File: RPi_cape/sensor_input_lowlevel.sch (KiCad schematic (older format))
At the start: 37 parts, among them U17 LM2903, U4 AD8552A

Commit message: Admin (naming, license), improvements based on testing
Updated name on schematic, PCB silkscreen
Added 3 mounting holes on inside area of board for better mechanical robustness
Removed extra unused pressure sensor barb packages from library
Fixed Phoenix spring connector footprints, and added 3D models from Phoenix website
Added 3D models to TE encoder connector footprints, QFP-100 for CPLD, and 5019 testpoint
Changed DIAG_EN pin connection from valve drivers from +24V (too high) to +3.3V
Added CERN licensing terms
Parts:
- TP20: footprint TestPoint:TestPoint_Keystone_5019_Minature -> Ventilator:TestPoint_Keystone_5019_Minature
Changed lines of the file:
@@
 encoding utf-8
 Sheet 5 15
-Title "Raspberry Pi Hat for JamVent Adaptation"
+Title "GlobalVent Stand-Alone Controller"
 Date ""
-Rev "1.9"
-Comp "US JamVent Team"
-Comment1 "Don Straney"
-Comment2 ""
+Rev "1.10"
+Comp "US GlobalVent Team"
+Comment1 "Licensed under CERN-OHL-S v2"
+Comment2 "Don Straney"
 Comment3 ""
 Comment4 ""
@@
 F 0 "TP20" H 2500 7300 50  0000 R CNN
 F 1 "TestPoint_Flag" H 2456 7203 50  0001 R CNN
-F 2 "TestPoint:TestPoint_Keystone_5019_Minature" H 2700 7200 50  0001 C CNN
+F 2 "Ventilator:TestPoint_Keystone_5019_Minature" H 2700 7200 50  0001 C CNN
 F 3 "~" H 2700 7200 50  0001 C CNN
 F 4 "Keystone" H 2500 7200 50  0001 C CNN "Manufacturer"

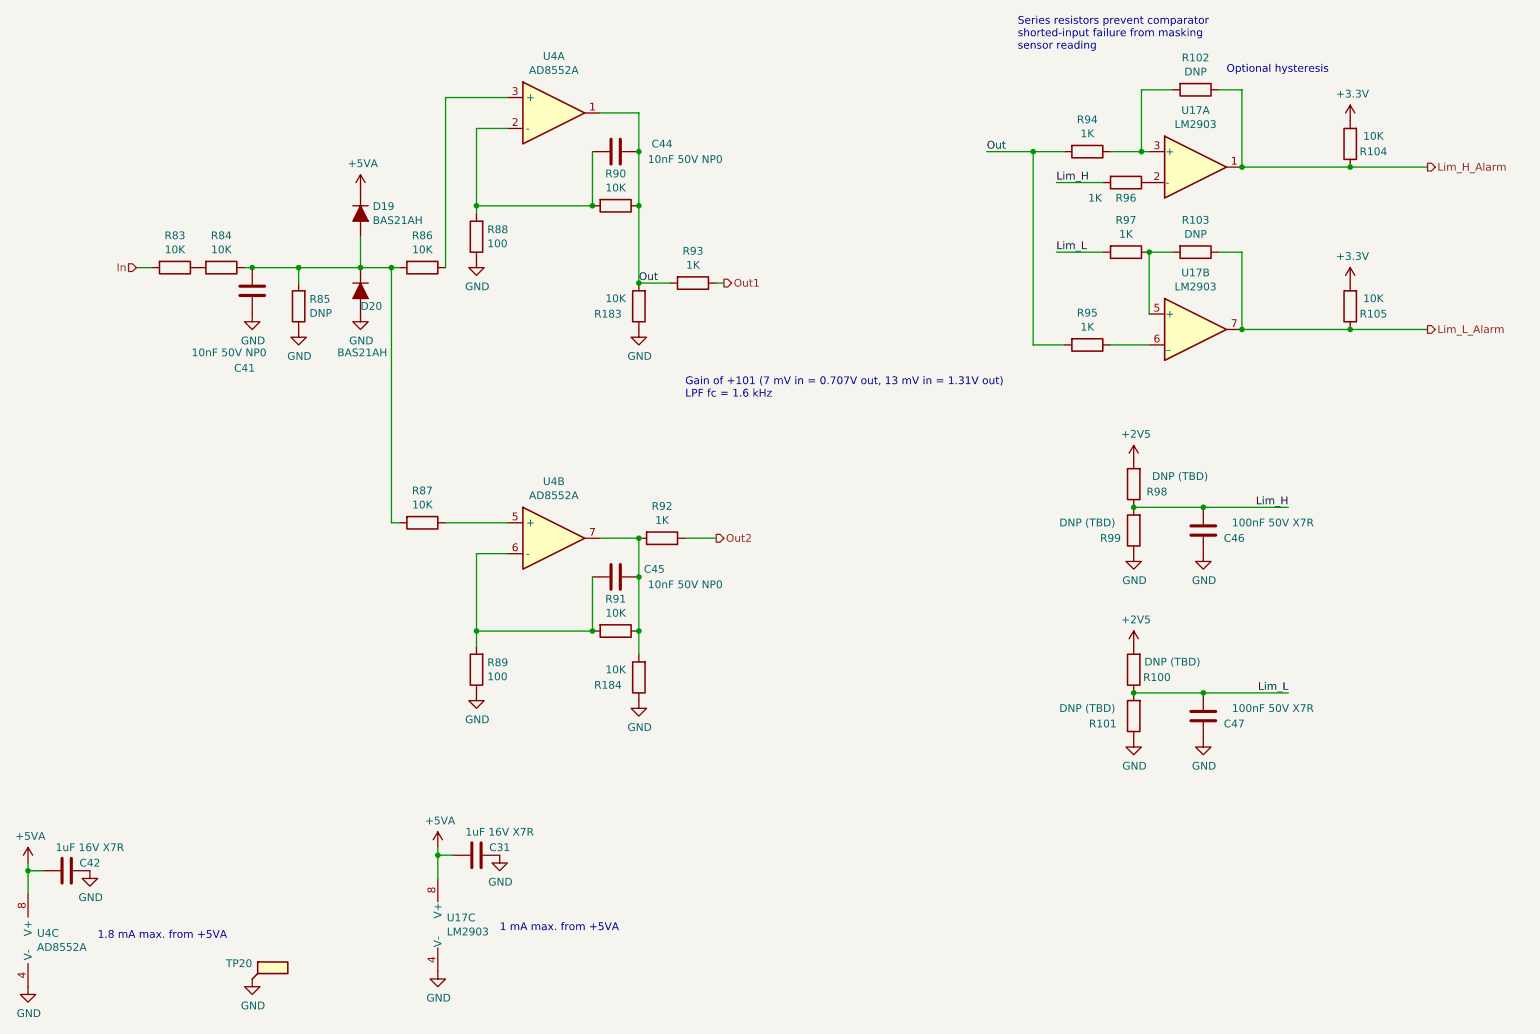
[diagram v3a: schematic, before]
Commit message: Design update based on changed software/firmware/pneumatics reqs
Swapped Max V CPLD for Max 10 FPGA
Removed +1.8V regulator and monitoring (in power-down alarm) because Max 10 FPGA has internal regulator
Changed FPGA's valve-enable pull-downs from 1K to 10K because Max 10 floats the outputs during power-up/programming (instead of Max V's internal pull-ups)
Changed low-pressure sensor from BMP388 to MS5607 for more manufacturable footprint / high availability, and moved all digital pressure sensors to daughterboard for repairability
Changed single op-amps in analog pressure sensor inputs / valve motion detect circuits to TLV6001 for better bias current, correct footprint
Removed excessive DNP components in analog pressure sensor inputs to ease routing with new op-amps
Added double-inverted hysteresis circuit to valve motion detect that won't drive U38's '+' input above the rail and cause latchup
Added optional pull-down resistors to valve-motiion-detect op-amps to allow output voltages to swing to zero
Added optional filter caps to ADC sensor inputs
Added pull-down to O2 sensor input for testing with sensor unplugged
Increased ADC input resistors (in analog sensor inputs) from 1K to 3.3K to avoid "lifting" +3.3V rail voltage in case of fault
Increased hole sizes to 3.7 mm for fitting #6 screws, to match some threaded vibration-damping bumpers from Joost
Fixed F.Fab-layer component reference text in custom footprints
Updated manufacturing files
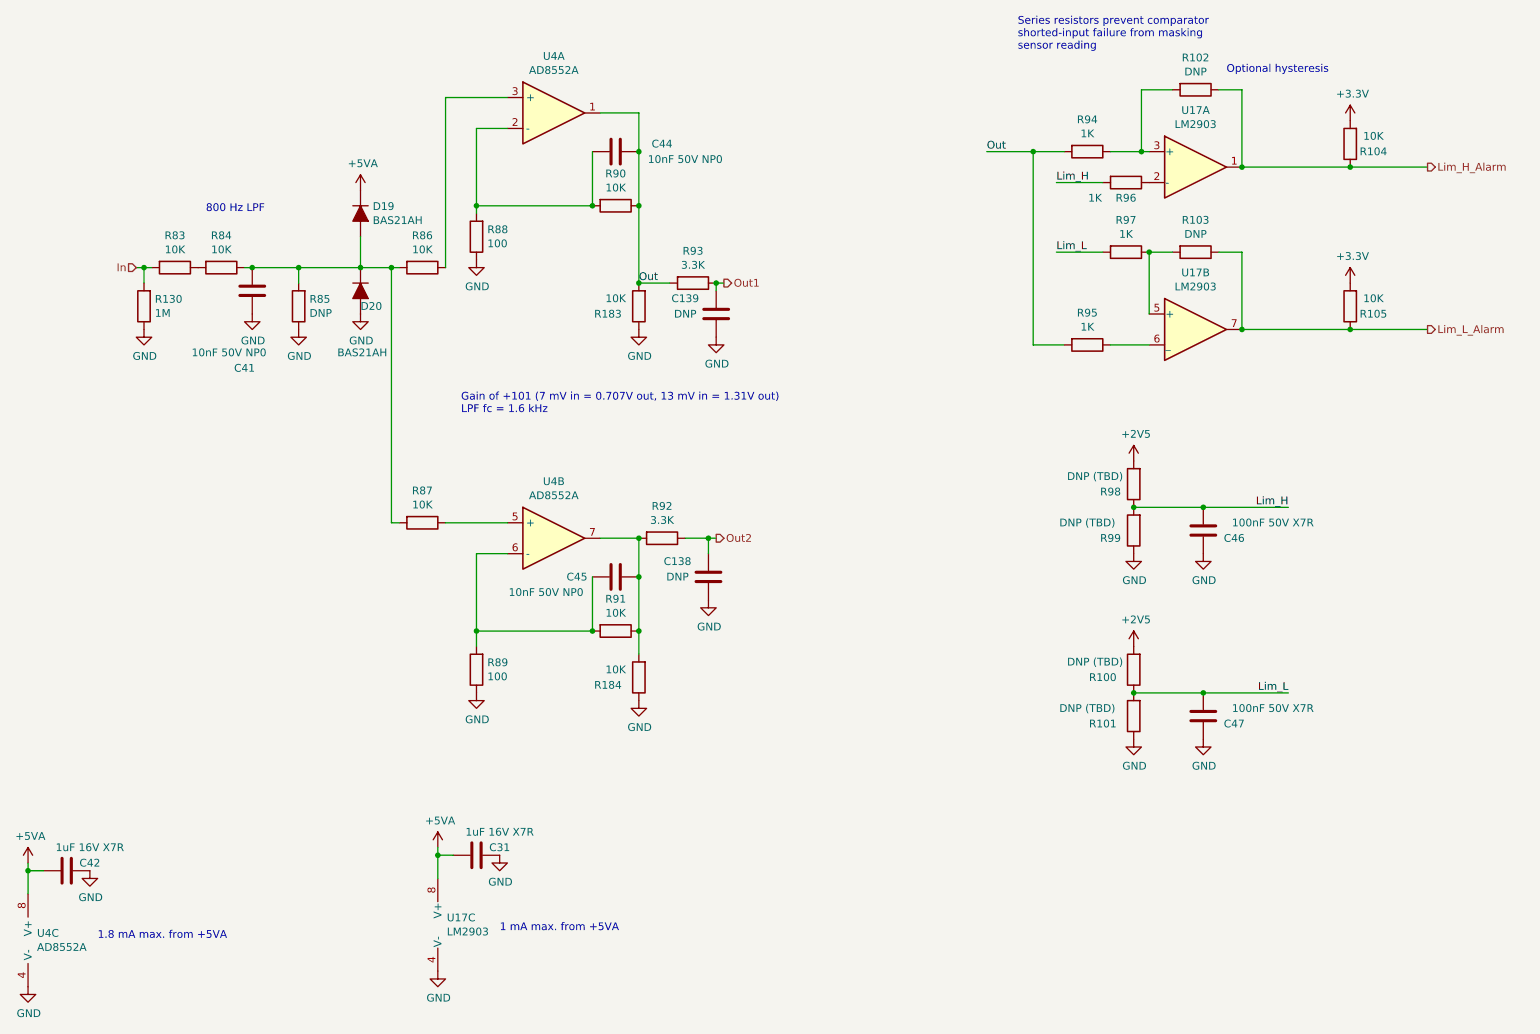
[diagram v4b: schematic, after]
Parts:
- removed TP20: TestPoint_Flag, Ventilator:TestPoint_Keystone_5019_Minature, symbol Connector:TestPoint_Flag
- added C138, C139: DNP, Capacitor_SMD:C_0603_1608Metric, symbol Device:C
- added R130: 1M, Resistor_SMD:R_1206_3216Metric, symbol Device:R
- R100, R101, R102, R103, R85, R98, R99: DNI (none) -> DNI
- R92, R93: value 1K -> 3.3K; Part Number RK73H2BTTD1001F -> RK73H2BTTD3301F
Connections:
- net GND: now also C138.1, C139.1, R130.1
- net In: now also R130.2
- net Out1: now also C139.2
- net Out2: now also C138.2
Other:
- note added: "800 Hz LPF"
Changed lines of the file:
@@
 $Descr A4 11693 8268
 encoding utf-8
-Sheet 5 15
+Sheet 5 13
 Title "GlobalVent Stand-Alone Controller"
 Date ""
-Rev "1.10"
+Rev "1.11"
 Comp "US GlobalVent Team"
 Comment1 "Licensed under CERN-OHL-S v2"
@@
 AR Path="/5E8A4ABF/5E8C0FEC" Ref="C?"  Part="1"
 AR Path="/5E8AA959/5E8C0FEC" Ref="C45"  Part="1"
-F 0 "C45" V 4800 4850 50  0000 C CNN
-F 1 "10nF 50V NP0" V 4900 5050 50  0000 C CNN
+F 0 "C45" V 4850 4350 50  0000 C CNN
+F 1 "10nF 50V NP0" V 4950 4150 50  0000 C CNN
 F 2 "Capacitor_SMD:C_0603_1608Metric" H 4888 4450 50  0001 C CNN
 F 3 "~" H 4850 4600 50  0001 C CNN
@@
 F 2 "Resistor_SMD:R_1206_3216Metric" V 2730 2850 50  0001 C CNN
 F 3 "~" H 2800 2850 50  0001 C CNN
+F 4 "DNI" H 2800 2850 50  0001 C CNN "DNI"
 	1    2800 2850
 	-1   0    0    1
@@
 In
 Wire Wire Line
-	1750 2600 1850 2600
+	1750 2600 1800 2600
 Text HLabel 5550 2700 2    50   Output ~ 0
 Out1
@@
 AR Path="/5E8AA959/5E8C10A8" Ref="R93"  Part="1"
 F 0 "R93" V 5143 2700 50  0000 C CNN
-F 1 "1K" V 5234 2700 50  0000 C CNN
+F 1 "3.3K" V 5234 2700 50  0000 C CNN
 F 2 "Resistor_SMD:R_1206_3216Metric" V 5280 2700 50  0001 C CNN
 F 3 "~" H 5350 2700 50  0001 C CNN
 F 4 "KOA Speer" H 5350 2700 50  0001 C CNN "Manufacturer"
-F 5 "RK73H2BTTD1001F" H 5350 2700 50  0001 C CNN "Part Number"
+F 5 "RK73H2BTTD3301F" H 5350 2700 50  0001 C CNN "Part Number"
 	1    5350 2700
 	0    1    1    0
@@
 AR Path="/5E8AA959/5E8C10AF" Ref="R92"  Part="1"
 F 0 "R92" V 4943 4350 50  0000 C CNN
-F 1 "1K" V 5034 4350 50  0000 C CNN
+F 1 "3.3K" V 5034 4350 50  0000 C CNN
 F 2 "Resistor_SMD:R_1206_3216Metric" V 5080 4350 50  0001 C CNN
 F 3 "~" H 5150 4350 50  0001 C CNN
 F 4 "KOA Speer" H 5150 4350 50  0001 C CNN "Manufacturer"
-F 5 "RK73H2BTTD1001F" H 5150 4350 50  0001 C CNN "Part Number"
+F 5 "RK73H2BTTD3301F" H 5150 4350 50  0001 C CNN "Part Number"
 	1    5150 4350
 	0    1    1    0
@@
 Connection ~ 5000 4350
 Wire Wire Line
-	5300 4350 5500 4350
+	5300 4350 5450 4350
 Wire Wire Line
 	5500 2700 5550 2700
-Text Notes 5300 3450 0    50   ~ 0
+Text Notes 3850 3550 0    50   ~ 0
 Gain of +101 (7 mV in = 0.707V out, 13 mV in = 1.31V out)\nLPF fc = 1.6 kHz
 $Comp
@@
 F 2 "Resistor_SMD:R_1206_3216Metric" V 8530 1450 50  0001 C CNN
 F 3 "~" H 8600 1450 50  0001 C CNN
+F 4 "DNI" H 8600 1450 50  0001 C CNN "DNI"
 	1    8600 1450
 	0    1    1    0
@@
 F 2 "Resistor_SMD:R_1206_3216Metric" V 8530 2500 50  0001 C CNN
 F 3 "~" H 8600 2500 50  0001 C CNN
+F 4 "DNI" H 8600 2500 50  0001 C CNN "DNI"
 	1    8600 2500
 	0    1    1    0
@@
 AR Path="/5E8A4ABF/5EDD8202" Ref="R?"  Part="1"
 AR Path="/5E8AA959/5EDD8202" Ref="R98"  Part="1"
-F 0 "R98" H 8050 4050 50  0000 C CNN
-F 1 "DNP (TBD)" H 7900 3950 50  0000 C CNN
+F 0 "R98" H 8350 4050 50  0000 C CNN
+F 1 "DNP (TBD)" H 8450 3950 50  0000 C CNN
 F 2 "Resistor_SMD:R_1206_3216Metric" V 8130 4000 50  0001 C CNN
 F 3 "~" H 8200 4000 50  0001 C CNN
+F 4 "DNI" H 8200 4000 50  0001 C CNN "DNI"
 	1    8200 4000
 	-1   0    0    1
@@
 F 2 "Resistor_SMD:R_1206_3216Metric" V 8130 4300 50  0001 C CNN
 F 3 "~" H 8200 4300 50  0001 C CNN
+F 4 "DNI" H 8200 4300 50  0001 C CNN "DNI"
 	1    8200 4300
 	-1   0    0    1
@@
 AR Path="/5E8A4ABF/5EDD822B" Ref="R?"  Part="1"
 AR Path="/5E8AA959/5EDD822B" Ref="R100"  Part="1"
-F 0 "R100" H 8050 5250 50  0000 C CNN
-F 1 "DNP (TBD)" H 7950 5150 50  0000 C CNN
+F 0 "R100" H 8400 5250 50  0000 C CNN
+F 1 "DNP (TBD)" H 8450 5150 50  0000 C CNN
 F 2 "Resistor_SMD:R_1206_3216Metric" V 8130 5200 50  0001 C CNN
 F 3 "~" H 8200 5200 50  0001 C CNN
+F 4 "DNI" H 8200 5200 50  0001 C CNN "DNI"
 	1    8200 5200
 	-1   0    0    1
@@
 F 2 "Resistor_SMD:R_1206_3216Metric" V 8130 5500 50  0001 C CNN
 F 3 "~" H 8200 5500 50  0001 C CNN
+F 4 "DNI" H 8200 5500 50  0001 C CNN "DNI"
 	1    8200 5500
 	-1   0    0    1
@@
 Out
 $Comp
-L Connector:TestPoint_Flag TP?
-U 1 1 5F6700EA
-P 2500 7200
-AR Path="/5F6700EA" Ref="TP?"  Part="1"
-AR Path="/5E8AA959/5F6700EA" Ref="TP20"  Part="1"
-F 0 "TP20" H 2500 7300 50  0000 R CNN
-F 1 "TestPoint_Flag" H 2456 7203 50  0001 R CNN
-F 2 "Ventilator:TestPoint_Keystone_5019_Minature" H 2700 7200 50  0001 C CNN
-F 3 "~" H 2700 7200 50  0001 C CNN
-F 4 "Keystone" H 2500 7200 50  0001 C CNN "Manufacturer"
-F 5 "5019" H 2500 7200 50  0001 C CNN "Part Number"
-	1    2500 7200
-	1    0    0    -1
-$EndComp
-$Comp
-L power:GND #PWR?
-U 1 1 5F6700F0
-P 2500 7200
-AR Path="/5F6700F0" Ref="#PWR?"  Part="1"
-AR Path="/5E8AFE9D/5F6700F0" Ref="#PWR?"  Part="1"
-AR Path="/5E8A4ABF/5F6700F0" Ref="#PWR?"  Part="1"
-AR Path="/5E8AA959/5F6700F0" Ref="#PWR0144"  Part="1"
-F 0 "#PWR0144" H 2500 6950 50  0001 C CNN
-F 1 "GND" H 2505 7027 50  0000 C CNN
-F 2 "" H 2500 7200 50  0001 C CNN
-F 3 "" H 2500 7200 50  0001 C CNN
-	1    2500 7200
-	1    0    0    -1
-$EndComp
-$Comp
 L Device:R R?
 U 1 1 5E90A00A
@@
 Text Notes 4100 6900 0    50   ~ 0
 1 mA max. from +5VA
+$Comp
+L Device:R R?
+U 1 1 5F97CE99
+P 1800 2850
+AR Path="/5F97CE99" Ref="R?"  Part="1"
+AR Path="/5E8AFE9D/5F97CE99" Ref="R?"  Part="1"
+AR Path="/5E8A4ABF/5F97CE99" Ref="R?"  Part="1"
+AR Path="/5E8AA959/5F97CE99" Ref="R130"  Part="1"
+F 0 "R130" H 1730 2804 50  0000 R CNN
+F 1 "1M" H 1730 2895 50  0000 R CNN
+F 2 "Resistor_SMD:R_1206_3216Metric" V 1730 2850 50  0001 C CNN
+F 3 "~" H 1800 2850 50  0001 C CNN
+F 4 "KOA Speer" H 1800 2850 50  0001 C CNN "Manufacturer"
+F 5 "RK73H2BTTD1004F" H 1800 2850 50  0001 C CNN "Part Number"
+	1    1800 2850
+	-1   0    0    1
+$EndComp
+$Comp
+L power:GND #PWR?
+U 1 1 5F97D262
+P 1800 3000
+AR Path="/5F97D262" Ref="#PWR?"  Part="1"
+AR Path="/5E8AFE9D/5F97D262" Ref="#PWR?"  Part="1"
+AR Path="/5E8A4ABF/5F97D262" Ref="#PWR?"  Part="1"
+AR Path="/5E8AA959/5F97D262" Ref="#PWR0250"  Part="1"
+F 0 "#PWR0250" H 1800 2750 50  0001 C CNN
+F 1 "GND" H 1805 2827 50  0000 C CNN
+F 2 "" H 1800 3000 50  0001 C CNN
+F 3 "" H 1800 3000 50  0001 C CNN
+	1    1800 3000
+	1    0    0    -1
+$EndComp
+Wire Wire Line
+	1800 2700 1800 2600
+Connection ~ 1800 2600
+Wire Wire Line
+	1800 2600 1850 2600
+Text Notes 2200 2250 0    50   ~ 0
+800 Hz LPF
+$Comp
+L Device:C C?
+U 1 1 5F3D5CAE
+P 5500 2900
+AR Path="/5F3D5CAE" Ref="C?"  Part="1"
+AR Path="/5E8AFE9D/5F3D5CAE" Ref="C?"  Part="1"
+AR Path="/5E8A4ABF/5F3D5CAE" Ref="C?"  Part="1"
+AR Path="/5E8AA959/5F3D5CAE" Ref="C139"  Part="1"
+F 0 "C139" H 5700 2800 50  0000 C CNN
+F 1 "DNP" H 5700 2900 50  0000 C CNN
+F 2 "Capacitor_SMD:C_0603_1608Metric" H 5538 2750 50  0001 C CNN
+F 3 "~" H 5500 2900 50  0001 C CNN
+F 4 "DNI" H 5500 2900 50  0001 C CNN "DNI"
+	1    5500 2900
+	-1   0    0    1
+$EndComp
+$Comp
+L power:GND #PWR?
+U 1 1 5F3D5CB4
+P 5500 3050
+AR Path="/5F3D5CB4" Ref="#PWR?"  Part="1"
+AR Path="/5E8AA959/5F3D5CB4" Ref="#PWR0408"  Part="1"
+F 0 "#PWR0408" H 5500 2800 50  0001 C CNN
+F 1 "GND" H 5505 2877 50  0000 C CNN
+F 2 "" H 5500 3050 50  0001 C CNN
+F 3 "" H 5500 3050 50  0001 C CNN
+	1    5500 3050
+	1    0    0    -1
+$EndComp
+Wire Wire Line
+	5500 2750 5500 2700
+Connection ~ 5500 2700
+$Comp
+L Device:C C?
+U 1 1 5F3E6F63
+P 5450 4600
+AR Path="/5F3E6F63" Ref="C?"  Part="1"
+AR Path="/5E8AFE9D/5F3E6F63" Ref="C?"  Part="1"
+AR Path="/5E8A4ABF/5F3E6F63" Ref="C?"  Part="1"
+AR Path="/5E8AA959/5F3E6F63" Ref="C138"  Part="1"
+F 0 "C138" H 5650 4500 50  0000 C CNN
+F 1 "DNP" H 5650 4600 50  0000 C CNN
+F 2 "Capacitor_SMD:C_0603_1608Metric" H 5488 4450 50  0001 C CNN
+F 3 "~" H 5450 4600 50  0001 C CNN
+F 4 "DNI" H 5450 4600 50  0001 C CNN "DNI"
+	1    5450 4600
+	-1   0    0    1
+$EndComp
+$Comp
+L power:GND #PWR?
+U 1 1 5F3E6F69
+P 5450 4750
+AR Path="/5F3E6F69" Ref="#PWR?"  Part="1"
+AR Path="/5E8AA959/5F3E6F69" Ref="#PWR0409"  Part="1"
+F 0 "#PWR0409" H 5450 4500 50  0001 C CNN
+F 1 "GND" H 5455 4577 50  0000 C CNN
+F 2 "" H 5450 4750 50  0001 C CNN
+F 3 "" H 5450 4750 50  0001 C CNN
+	1    5450 4750
+	1    0    0    -1
+$EndComp
+Wire Wire Line
+	5450 4450 5450 4350
+Connection ~ 5450 4350
+Wire Wire Line
+	5450 4350 5500 4350
 $EndSCHEMATC
